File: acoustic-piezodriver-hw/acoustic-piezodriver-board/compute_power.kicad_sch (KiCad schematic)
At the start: 28 parts, among them J301 Conn_02x06_Odd_Even, U10 NCE6005AS, U9 LM3478MM

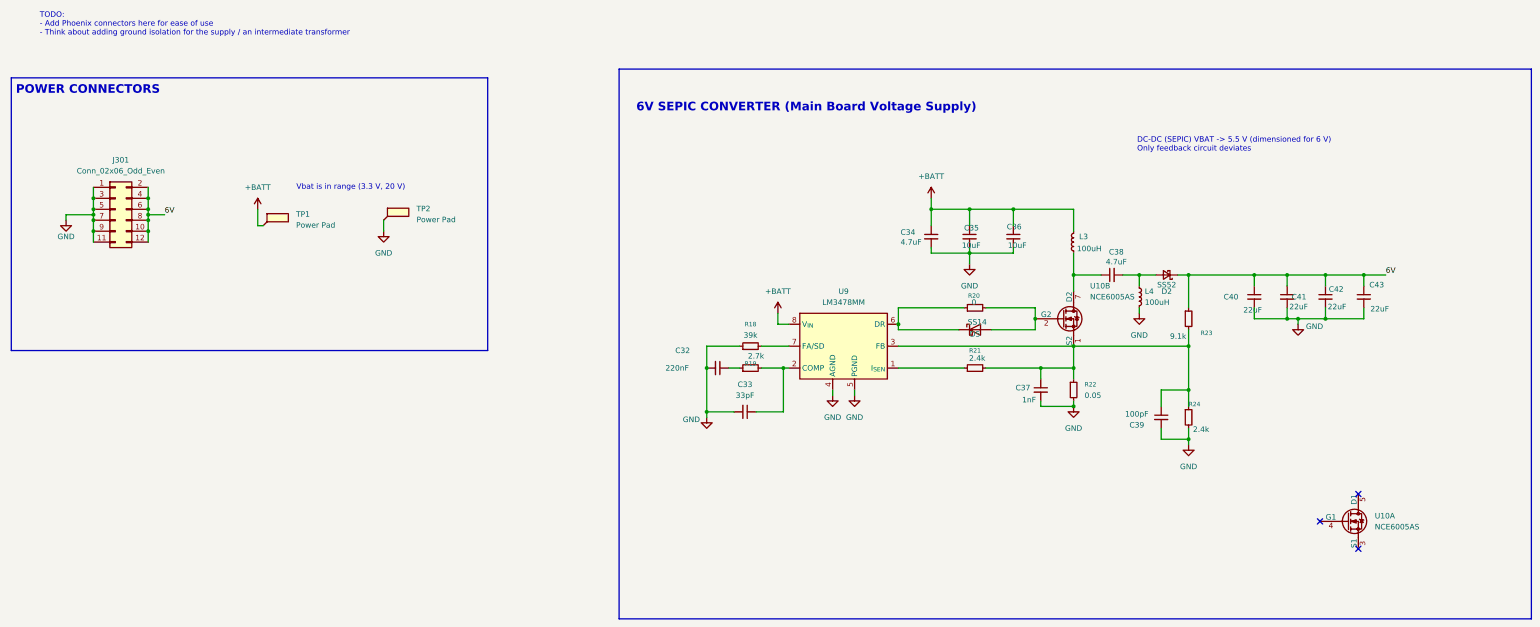
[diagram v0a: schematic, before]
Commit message: [piezodriver] Reorganised piezodriver schematic (next) figure out output filtering
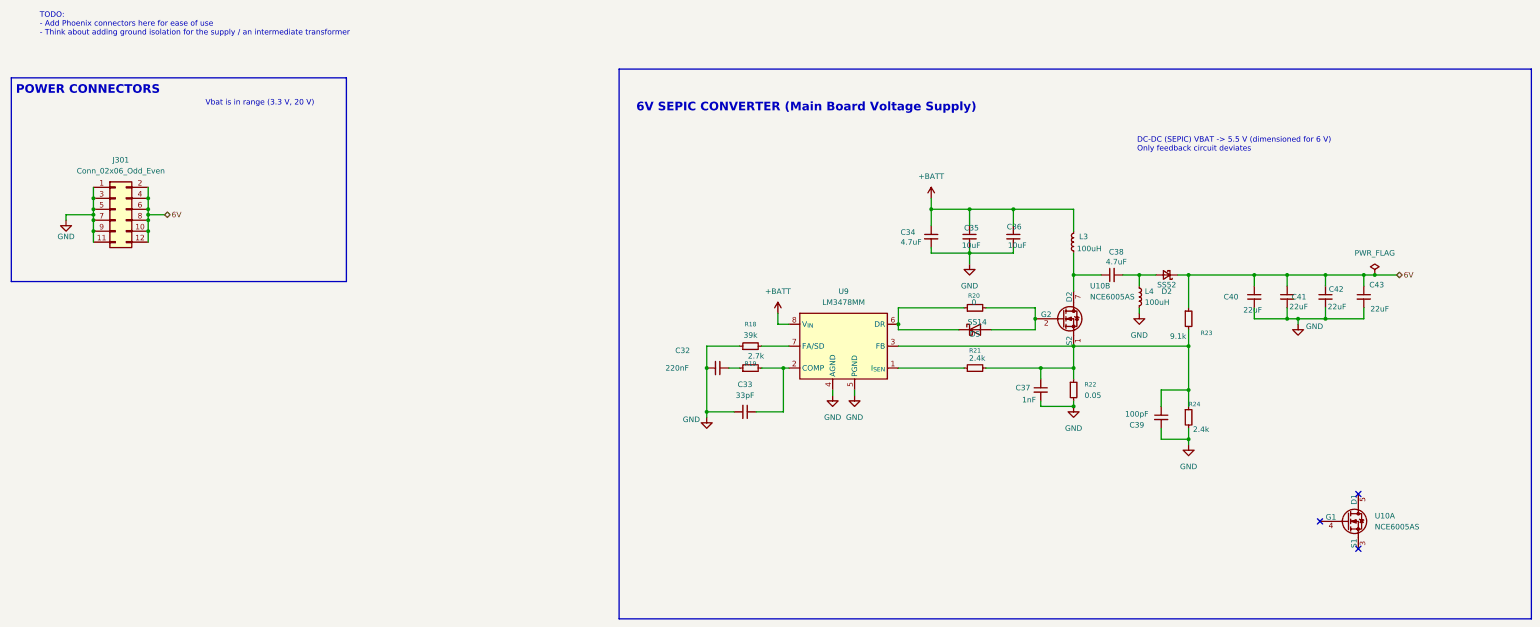
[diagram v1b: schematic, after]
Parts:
- removed TP1, TP2: Power Pad, TestPoint:TestPoint_Pad_4.0x4.0mm, symbol Connector:TestPoint_Flag
